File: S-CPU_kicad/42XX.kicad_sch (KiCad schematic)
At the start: 161 parts, among them U34 OR_2, U35 OR_2, U36 OR_2, U37 OR_2, U6 MUX

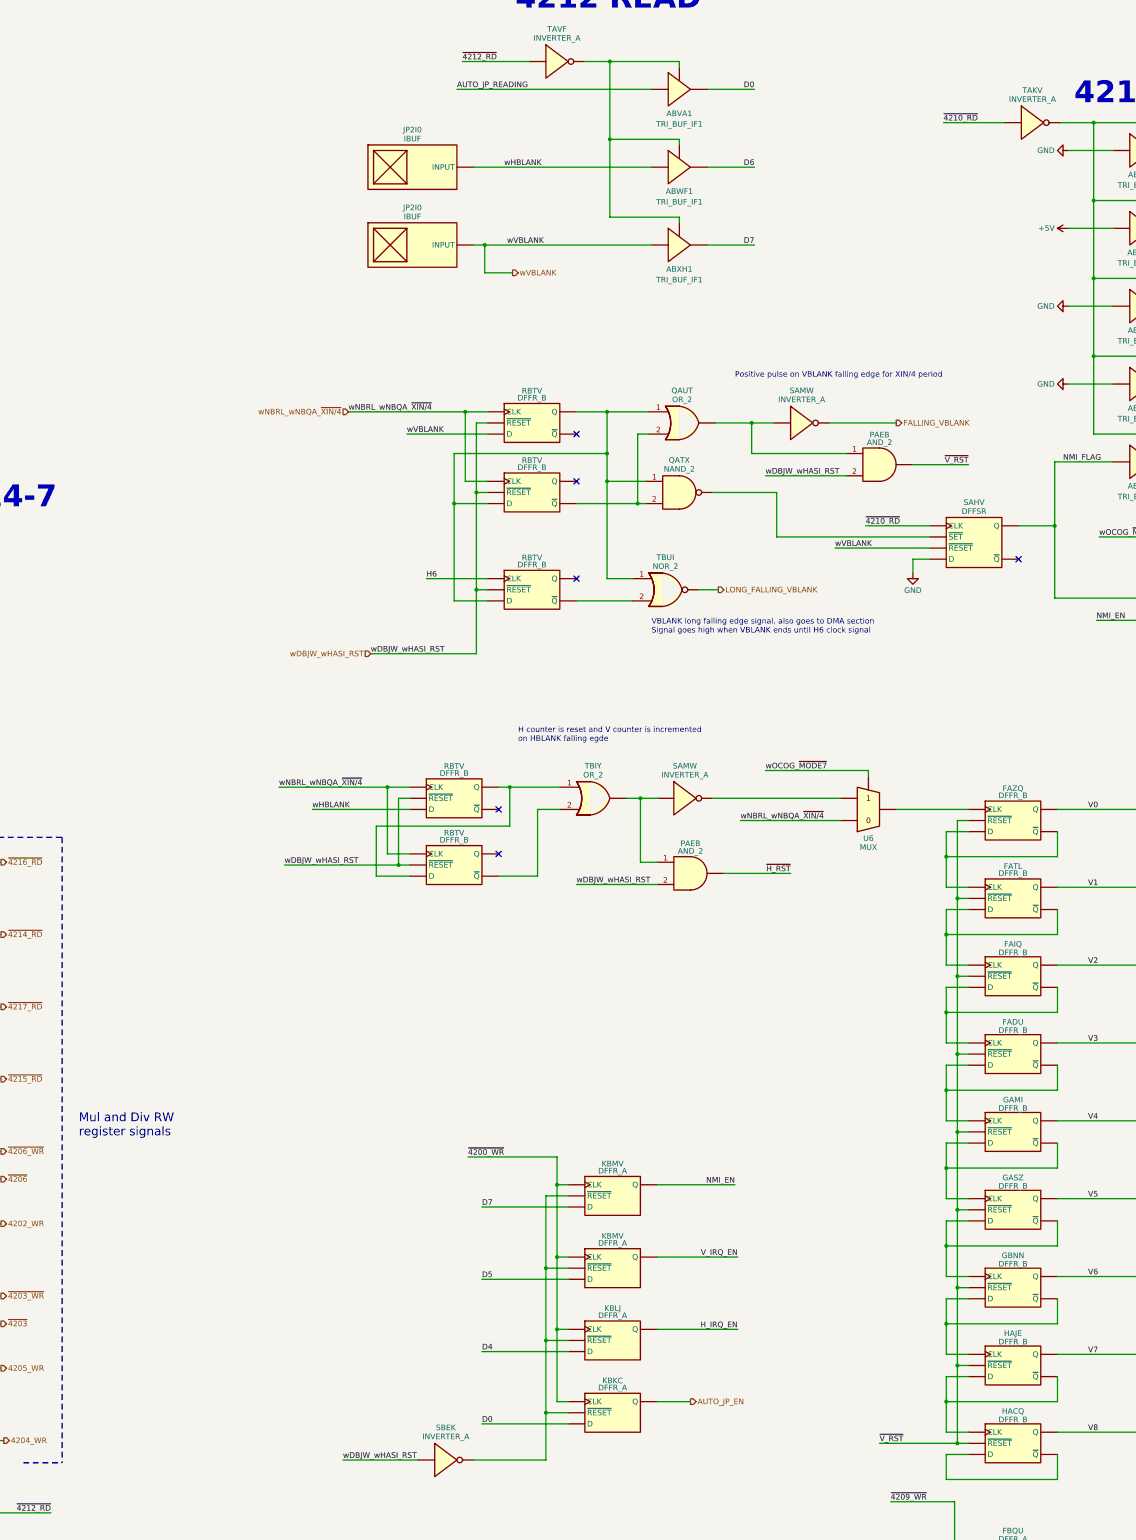
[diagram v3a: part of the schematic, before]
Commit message: Schematics tidying in progress.
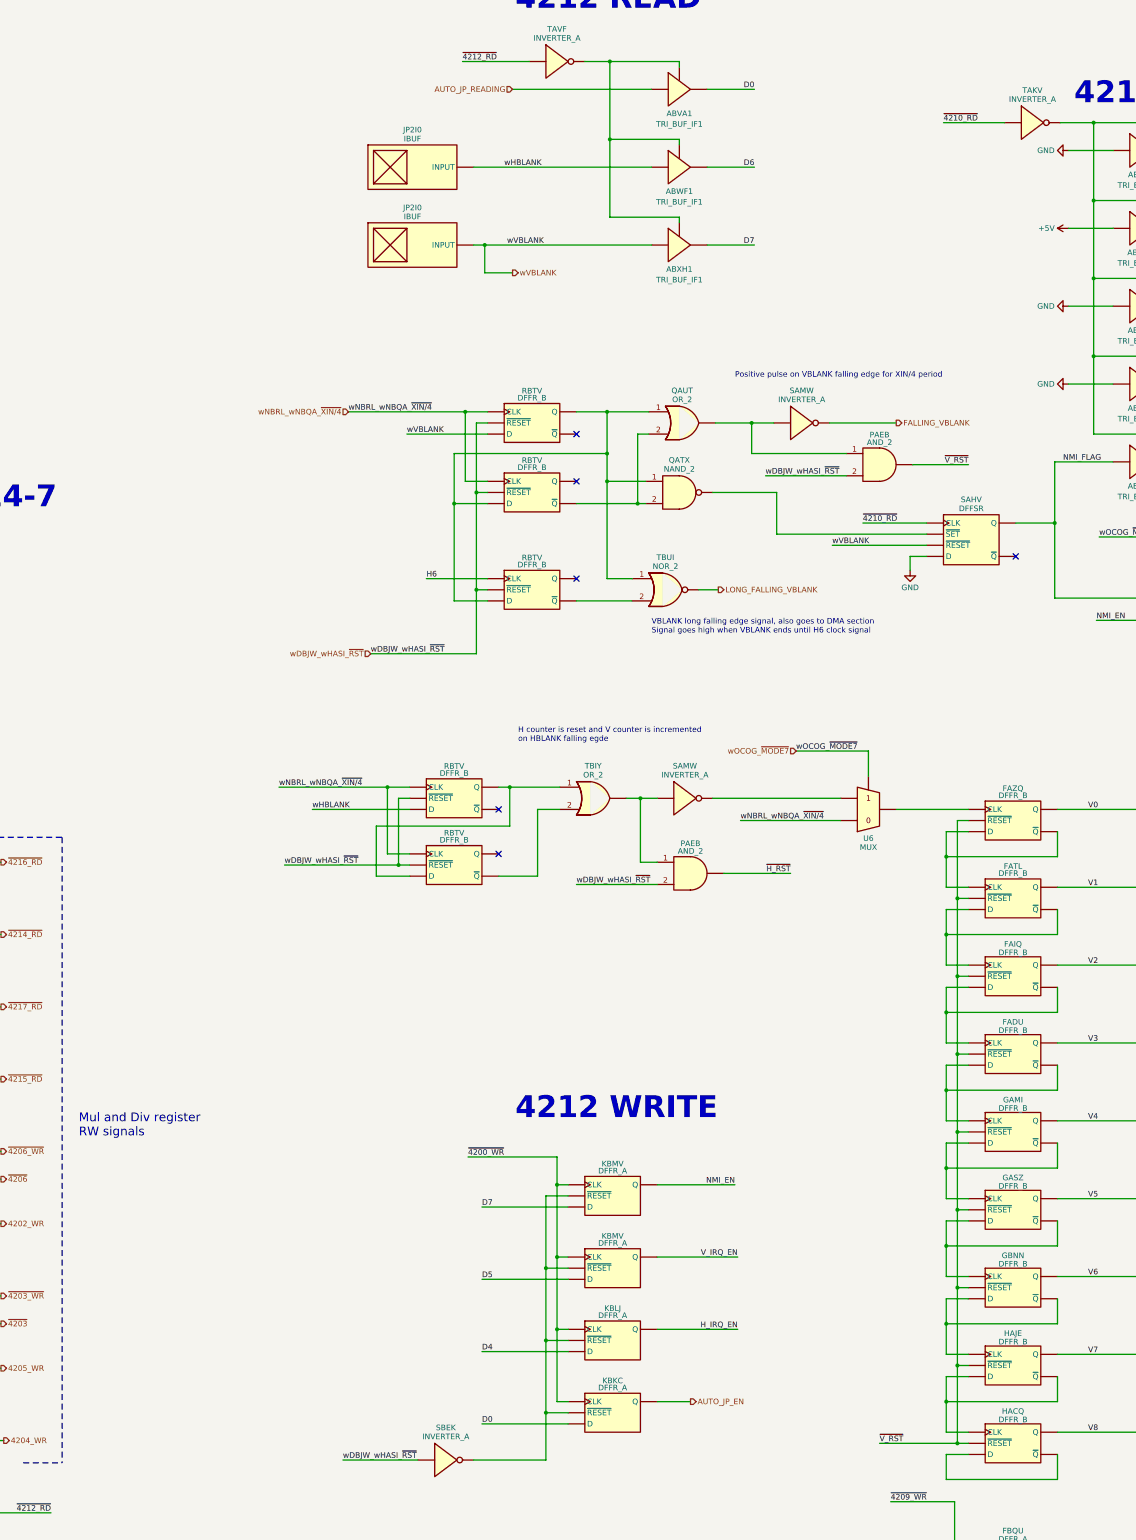
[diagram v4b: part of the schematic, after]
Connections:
- net wDBJW_wHASI_RST renamed wDBJW_wHASI_~{RST}
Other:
- note added: "4212 WRITE"
- note added: "Mul and Div register RW signals"
- note removed: "Mul and Div RW register signals"
- moved on the sheet: SAHV
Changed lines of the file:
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@@
   (title_block
     (title "SNES S-CPU Schematics ")
-    (date "2023-06-14")
+    (date "2023-10-19")
     (rev "0.1")
     (company "Author: Regis Galland")
@@
   (junction (at 125.095 382.27) (diameter 0) (color 0 0 0 0)
   )
+  (junction (at 434.975 158.75) (diameter 0) (color 0 0 0 0)
+  )
   (junction (at 132.715 302.26) (diameter 0) (color 0 0 0 0)
   )
@@
   (junction (at 410.21 288.29) (diameter 0) (color 0 0 0 0)
   )
-  (junction (at 434.975 159.385) (diameter 0) (color 0 0 0 0)
-  )
   (junction (at 663.575 298.45) (diameter 0) (color 0 0 0 0)
   )
@@
   (no_connect (at 307.975 234.315))
   (no_connect (at 415.29 489.585))
-  (no_connect (at 426.72 167.005))
+  (no_connect (at 426.085 166.37))
   (bus_entry (at 71.755 209.55) (size -2.54 2.54)
     (stroke (width 0) (type default))
@@
     (stroke (width 0) (type default))
   )
-  (wire (pts (xy 402.59 170.18) (xy 402.59 167.005))
+  (wire (pts (xy 401.955 169.545) (xy 401.955 166.37))
     (stroke (width 0) (type default))
   )
@@
     (stroke (width 0) (type default))
   )
-  (wire (pts (xy 371.475 161.925) (xy 406.4 161.925))
+  (wire (pts (xy 371.475 161.29) (xy 405.765 161.29))
     (stroke (width 0) (type default))
   )
@@
     (stroke (width 0) (type default))
   )
-  (wire (pts (xy 434.975 159.385) (xy 426.72 159.385))
+  (wire (pts (xy 434.975 158.75) (xy 426.085 158.75))
     (stroke (width 0) (type default))
   )
@@
     (stroke (width 0) (type default))
   )
-  (wire (pts (xy 434.975 144.78) (xy 434.975 159.385))
+  (wire (pts (xy 434.975 144.78) (xy 434.975 158.75))
     (stroke (width 0) (type default))
   )
@@
     (stroke (width 0) (type default))
   )
-  (wire (pts (xy 368.935 215.265) (xy 392.43 215.265))
+  (wire (pts (xy 375.92 210.82) (xy 392.43 210.82))
     (stroke (width 0) (type default))
   )
@@
     (stroke (width 0) (type default))
   )
-  (wire (pts (xy 406.4 159.385) (xy 391.795 159.385))
+  (wire (pts (xy 405.765 158.75) (xy 391.16 158.75))
     (stroke (width 0) (type default))
   )
@@
     (stroke (width 0) (type default))
   )
-  (wire (pts (xy 371.475 151.765) (xy 371.475 161.925))
+  (wire (pts (xy 371.475 151.765) (xy 371.475 161.29))
     (stroke (width 0) (type default))
   )
@@
     (stroke (width 0) (type default))
   )
-  (wire (pts (xy 384.81 164.465) (xy 406.4 164.465))
+  (wire (pts (xy 384.175 163.83) (xy 405.765 163.83))
     (stroke (width 0) (type default))
   )
@@
     (stroke (width 0) (type default))
   )
-  (wire (pts (xy 434.975 159.385) (xy 434.975 175.895))
+  (wire (pts (xy 434.975 158.75) (xy 434.975 175.895))
     (stroke (width 0) (type default))
   )
@@
     (stroke (width 0) (type default))
   )
-  (wire (pts (xy 402.59 167.005) (xy 406.4 167.005))
+  (wire (pts (xy 401.955 166.37) (xy 405.765 166.37))
     (stroke (width 0) (type default))
   )
@@
     (stroke (width 0) (type default))
   )
-  (wire (pts (xy 392.43 215.265) (xy 392.43 216.535))
+  (wire (pts (xy 392.43 210.82) (xy 392.43 216.535))
     (stroke (width 0) (type default))
   )
@@
     (stroke (width 0) (type default))
   )
-  (wire (pts (xy 298.45 59.69) (xy 342.9 59.69))
+  (wire (pts (xy 311.15 59.69) (xy 342.9 59.69))
     (stroke (width 0) (type default))
   )
@@
     (effects (font (size 5 5) (thickness 1) bold) (justify left bottom))
   )
+  (text "4212 WRITE" (at 311.785 295.275 0)
+    (effects (font (size 5 5) (thickness 1) bold) (justify left bottom))
+  )
   (text "Positive pulse on VBLANK falling edge for XIN/4 period"
     (at 361.95 125.73 0)
@@
     (effects (font (size 5 5) (thickness 1) bold) (justify left bottom))
   )
-  (text "Mul and Div RW\nregister signals" (at 212.09 299.085 0)
+  (text "Mul and Div register\nRW signals" (at 212.09 299.085 0)
     (effects (font (size 2 2)) (justify left bottom))
   )
@@
     (effects (font (size 1.27 1.27)) (justify right bottom))
   )
-  (label "~{4210_RD}" (at 391.795 159.385 0) (fields_autoplaced)
+  (label "~{4210_RD}" (at 391.16 158.75 0) (fields_autoplaced)
     (effects (font (size 1.27 1.27)) (justify left bottom))
   )
@@
     (effects (font (size 1.27 1.27)) (justify left bottom))
   )
-  (label "wDBJW_wHASI_RST" (at 368.935 147.955 0) (fields_autoplaced)
+  (label "wDBJW_wHASI_~{RST}" (at 368.935 147.955 0) (fields_autoplaced)
     (effects (font (size 1.27 1.27)) (justify left bottom))
   )
@@
     (effects (font (size 1.27 1.27)) (justify left bottom))
   )
-  (label "wVBLANK" (at 384.81 164.465 0) (fields_autoplaced)
+  (label "wVBLANK" (at 384.175 163.83 0) (fields_autoplaced)
     (effects (font (size 1.27 1.27)) (justify left bottom))
   )
@@
     (effects (font (size 1.27 1.27)) (justify left bottom))
   )
-  (label "wDBJW_wHASI_RST" (at 278.765 188.595 0) (fields_autoplaced)
+  (label "wDBJW_wHASI_~{RST}" (at 278.765 188.595 0) (fields_autoplaced)
     (effects (font (size 1.27 1.27)) (justify left bottom))
   )
@@
     (effects (font (size 1.27 1.27)) (justify right bottom))
   )
-  (label "wOCOG_~{MODE7}" (at 368.935 215.265 0) (fields_autoplaced)
+  (label "wOCOG_~{MODE7}" (at 375.92 210.82 0) (fields_autoplaced)
     (effects (font (size 1.27 1.27)) (justify left bottom))
   )
@@
     (effects (font (size 1.27 1.27)) (justify right bottom))
   )
-  (label "wDBJW_wHASI_RST" (at 272.415 372.745 0) (fields_autoplaced)
+  (label "wDBJW_wHASI_~{RST}" (at 272.415 372.745 0) (fields_autoplaced)
     (effects (font (size 1.27 1.27)) (justify left bottom))
   )
@@
     (effects (font (size 1.27 1.27)) (justify left bottom))
   )
-  (label "wDBJW_wHASI_RST" (at 325.755 241.3 0) (fields_autoplaced)
+  (label "wDBJW_wHASI_~{RST}" (at 325.755 241.3 0) (fields_autoplaced)
     (effects (font (size 1.27 1.27)) (justify left bottom))
   )
@@
     (effects (font (size 1.27 1.27)) (justify left bottom))
   )
-  (label "wDBJW_wHASI_RST" (at 259.08 236.855 0) (fields_autoplaced)
+  (label "wDBJW_wHASI_~{RST}" (at 259.08 236.855 0) (fields_autoplaced)
     (effects (font (size 1.27 1.27)) (justify left bottom))
   )
@@
     (effects (font (size 1.27 1.27)) (justify left bottom))
   )
-  (label "AUTO_JP_READING" (at 298.45 59.69 0) (fields_autoplaced)
-    (effects (font (size 1.27 1.27)) (justify left bottom))
-  )
   (label "~{4216}" (at 168.91 233.68 180) (fields_autoplaced)
     (effects (font (size 1.27 1.27)) (justify right bottom))
@@
     (effects (font (size 1.27 1.27)) (justify left))
   )
+  (hierarchical_label "wOCOG_~{MODE7}" (shape input) (at 375.92 210.82 180) (fields_autoplaced)
+    (effects (font (size 1.27 1.27)) (justify right))
+  )
+  (hierarchical_label "AUTO_JP_READING" (shape input) (at 311.15 59.69 180) (fields_autoplaced)
+    (effects (font (size 1.27 1.27)) (justify right))
+  )
   (hierarchical_label "wNBRL_wNBQA_~{XIN{slash}4}" (shape input) (at 273.685 133.35 180) (fields_autoplaced)
     (effects (font (size 1.27 1.27)) (justify right))
@@
     (effects (font (size 1.27 1.27)) (justify left))
   )
-  (hierarchical_label "wDBJW_wHASI_RST" (shape input) (at 278.765 188.595 180) (fields_autoplaced)
+  (hierarchical_label "wDBJW_wHASI_~{RST}" (shape input) (at 278.765 188.595 180) (fields_autoplaced)
     (effects (font (size 1.27 1.27)) (justify right))
   )
@@
     )
   )
-  (symbol (lib_id "Ricoh_Cells:DFFSR") (at 416.56 163.195 0) (unit 1)
+  (symbol (lib_id "Ricoh_Cells:DFFSR") (at 415.925 162.56 0) (unit 1)
     (in_bom yes) (on_board yes) (dnp no) (fields_autoplaced)
-    (property "Reference" "SAHV" (at 416.56 154.027 0)
+    (property "Reference" "SAHV" (at 415.925 153.392 0)
       (effects (font (size 1.27 1.27)))
     )
-    (property "Value" "DFFSR" (at 416.56 156.075 0)
+    (property "Value" "DFFSR" (at 415.925 155.44 0)
       (effects (font (size 1.27 1.27)))
     )
-    (property "Footprint" "" (at 416.56 163.195 0)
+    (property "Footprint" "" (at 415.925 162.56 0)
       (effects (font (size 1.27 1.27)) hide)
     )
-    (property "Datasheet" "http://iceboy.a-singer.de/doc/dmg_cells.html#dffsr" (at 416.56 172.72 0)
+    (property "Datasheet" "http://iceboy.a-singer.de/doc/dmg_cells.html#dffsr" (at 415.925 172.085 0)
       (effects (font (size 1.27 1.27)) hide)
     )
@@
     )
   )
-  (symbol (lib_id "power:GND") (at 402.59 170.18 0) (unit 1)
+  (symbol (lib_id "power:GND") (at 401.955 169.545 0) (unit 1)
     (in_bom yes) (on_board yes) (dnp no) (fields_autoplaced)
-    (property "Reference" "#PWR012" (at 402.59 176.53 0)
+    (property "Reference" "#PWR012" (at 401.955 175.895 0)
       (effects (font (size 1.27 1.27)) hide)
     )
-    (property "Value" "GND" (at 402.59 174.125 0)
+    (property "Value" "GND" (at 401.955 173.49 0)
       (effects (font (size 1.27 1.27)))
     )
-    (property "Footprint" "" (at 402.59 170.18 0)
+    (property "Footprint" "" (at 401.955 169.545 0)
       (effects (font (size 1.27 1.27)) hide)
     )
-    (property "Datasheet" "" (at 402.59 170.18 0)
+    (property "Datasheet" "" (at 401.955 169.545 0)
       (effects (font (size 1.27 1.27)) hide)
     )

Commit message: Big update on the hierarchical sheet. DMA section update too.
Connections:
- net H128-135 renamed ~{H128-135}
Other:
- note added: "32 Master cycles"
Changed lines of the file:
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@@
   (title_block
     (title "SNES S-CPU Schematics ")
-    (date "2023-10-19")
+    (date "2023-10-21")
     (rev "0.1")
     (company "Author: Regis Galland")
@@
   (junction (at 173.355 238.76) (diameter 0) (color 0 0 0 0)
   )
+  (junction (at 304.8 77.47) (diameter 0) (color 0 0 0 0)
+  )
   (junction (at 127.635 431.8) (diameter 0) (color 0 0 0 0)
   )
@@
     (stroke (width 0) (type default))
   )
+  (wire (pts (xy 304.8 83.82) (xy 311.15 83.82))
+    (stroke (width 0) (type default))
+  )
   (wire (pts (xy 122.555 393.7) (xy 122.555 377.19))
     (stroke (width 0) (type default))
@@
     (stroke (width 0) (type default))
   )
+  (wire (pts (xy 304.8 77.47) (xy 304.8 83.82))
+    (stroke (width 0) (type default))
+  )
   (wire (pts (xy 692.785 426.72) (xy 697.865 426.72))
     (stroke (width 0) (type default))
@@
     (stroke (width 0) (type default))
   )
+  (bus (pts (xy 704.85 228.6) (xy 723.9 228.6))
+    (stroke (width 0) (type default))
+  )
   (wire (pts (xy 142.875 354.33) (xy 147.32 354.33))
     (stroke (width 0) (type default))
@@
     (stroke (width 0) (type default))
   )
-  (wire (pts (xy 302.26 77.47) (xy 342.9 77.47))
+  (wire (pts (xy 302.26 77.47) (xy 304.8 77.47))
     (stroke (width 0) (type default))
   )
@@
     (stroke (width 0) (type default))
   )
+  (wire (pts (xy 304.8 77.47) (xy 342.9 77.47))
+    (stroke (width 0) (type default))
+  )
   (wire (pts (xy 725.805 288.29) (xy 725.805 351.79))
     (stroke (width 0) (type default))
@@
     (effects (font (size 1.27 1.27)) (justify left bottom))
   )
+  (text "32 Master cycles" (at 759.46 290.195 0)
+    (effects (font (size 1.27 1.27)) (justify left bottom))
+  )
   (text "4207/8 WRITE" (at 617.22 522.605 0)
     (effects (font (size 5 5) (thickness 1) bold) (justify left bottom))
@@
     (effects (font (size 1.27 1.27)) (justify right bottom))
   )
+  (label "H[0..8]" (at 704.85 228.6 0) (fields_autoplaced)
+    (effects (font (size 1.27 1.27)) (justify left bottom))
+  )
   (label "~{V_TIME}" (at 565.785 165.1 0) (fields_autoplaced)
     (effects (font (size 1.27 1.27)) (justify left bottom))
@@
     (effects (font (size 1.27 1.27)) (justify right bottom))
   )
-  (label "H128-135" (at 758.825 284.48 180) (fields_autoplaced)
-    (effects (font (size 1.27 1.27)) (justify right bottom))
-  )
   (label "V0" (at 442.595 224.155 0) (fields_autoplaced)
     (effects (font (size 1.27 1.27)) (justify left bottom))
@@
     (effects (font (size 1.27 1.27)) (justify left))
   )
-  (hierarchical_label "H128-135" (shape output) (at 761.365 284.48 0) (fields_autoplaced)
+  (hierarchical_label "~{H128-135}" (shape output) (at 761.365 284.48 0) (fields_autoplaced)
     (effects (font (size 1.27 1.27)) (justify left))
   )
@@
     (effects (font (size 1.27 1.27)) (justify right))
   )
+  (hierarchical_label "wHBLANK" (shape output) (at 311.15 83.82 0) (fields_autoplaced)
+    (effects (font (size 1.27 1.27)) (justify left))
+  )
   (hierarchical_label "~{4216_RD}" (shape output) (at 194.31 236.22 0) (fields_autoplaced)
     (effects (font (size 1.27 1.27)) (justify left))
@@
     (effects (font (size 1.27 1.27)) (justify right))
   )
+  (hierarchical_label "H[0..8]" (shape output) (at 723.9 228.6 0) (fields_autoplaced)
+    (effects (font (size 1.27 1.27)) (justify left))
+  )
   (hierarchical_label "4204_WR" (shape output) (at 194.945 368.3 0) (fields_autoplaced)
